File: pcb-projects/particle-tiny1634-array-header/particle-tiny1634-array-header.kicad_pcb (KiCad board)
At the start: 2 copper layers, 86.4 x 15.2 mm, 8 parts, among them P1 CHAIN1-TX, P2 CHAIN1-RX, P3 USB_A, P4 PWR-WEST, P5 PWR-EAST, P6 CHAIN2-TX, P7 CHAIN2-RX, P8 RS232

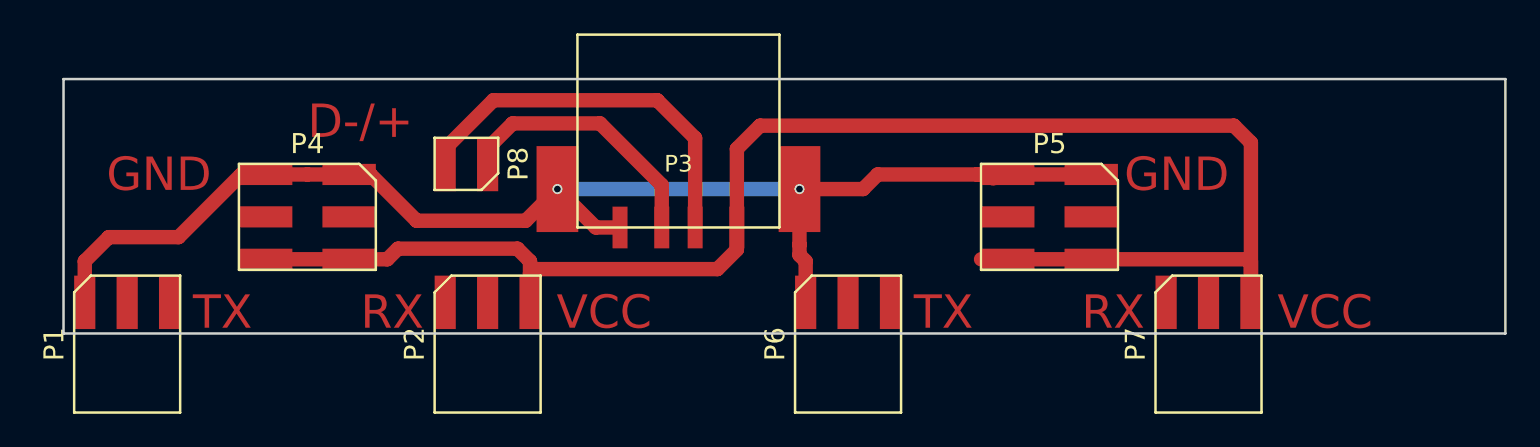
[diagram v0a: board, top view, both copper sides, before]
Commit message: minor edge cut alignment, added particle array
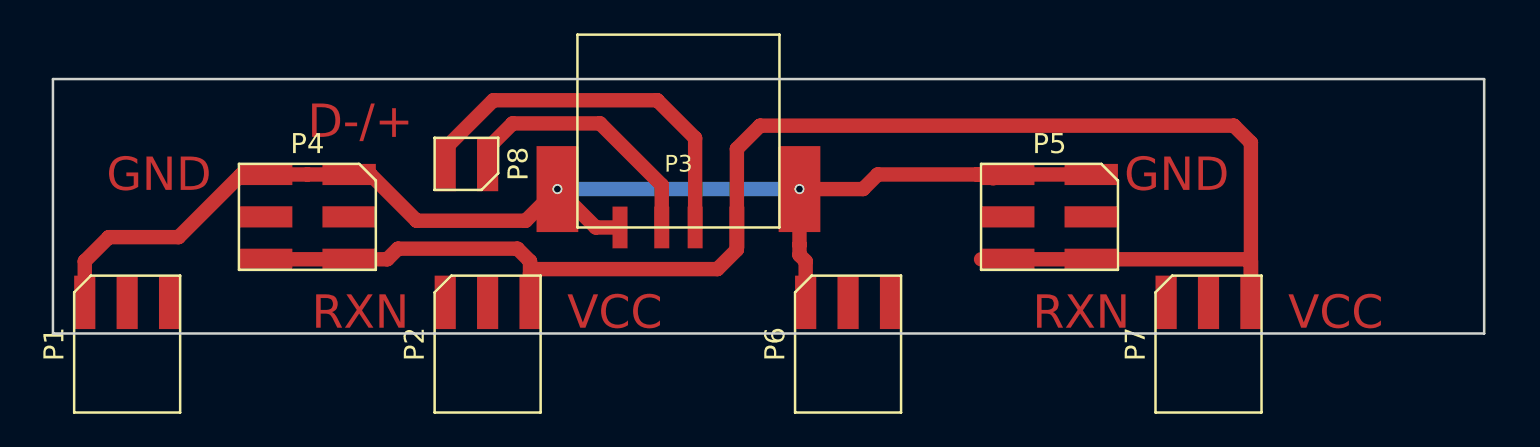
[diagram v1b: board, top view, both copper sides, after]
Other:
- board size 86.4 x 15.2 mm -> 85.7 x 15.2 mm
- board text added: "RXN"
- board text removed: "RX"
- board text removed: "TX"
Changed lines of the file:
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@@
     (links 16)
     (no_connects 0)
-    (area 27.864999 53.899999 114.375001 83.260001)
+    (area 25.98 50.909999 114.375001 74.355001)
     (thickness 1.6)
-    (drawings 13)
+    (drawings 11)
     (tracks 61)
     (zones 0)
@@
       (padsonsilk false)
       (subtractmaskfromsilk false)
-      (outputformat 1)
+      (outputformat 4)
       (mirror false)
-      (drillshape 1)
+      (drillshape 0)
       (scaleselection 1)
       (outputdirectory ""))
@@
     (effects (font (size 2 2) (thickness 0.4)))
   )
-  (gr_text RX (at 90.805 67.945) (layer F.Cu)
-    (effects (font (size 2 2) (thickness 0.4)))
-  )
-  (gr_text TX (at 80.645 67.945) (layer F.Cu)
-    (effects (font (size 2 2) (thickness 0.4)))
-  )
-  (gr_text RX (at 47.625 67.945) (layer F.Cu)
-    (effects (font (size 2 2) (thickness 0.4)))
-  )
-  (gr_text TX (at 37.465 67.945) (layer F.Cu)
-    (effects (font (size 2 2) (thickness 0.4)))
-  )
-  (gr_text VCC (at 60.325 67.945) (layer F.Cu)
+  (gr_text RXN (at 88.9 67.945) (layer F.Cu)
+    (effects (font (size 2 2) (thickness 0.4)))
+  )
+  (gr_text RXN (at 45.72 67.945) (layer F.Cu)
+    (effects (font (size 2 2) (thickness 0.4)))
+  )
+  (gr_text VCC (at 60.96 67.945) (layer F.Cu)
     (effects (font (size 2 2) (thickness 0.4)))
   )
@@
     (effects (font (size 2 2) (thickness 0.4)))
   )
-  (gr_text VCC (at 103.505 67.945) (layer F.Cu)
-    (effects (font (size 2 2) (thickness 0.4)))
-  )
-  (gr_line (start 27.94 53.975) (end 114.3 53.975) (layer Edge.Cuts) (width 0.15))
-  (gr_line (start 27.94 69.215) (end 114.3 69.215) (layer Edge.Cuts) (width 0.15))
-  (gr_line (start 114.3 69.215) (end 114.3 53.975) (layer Edge.Cuts) (width 0.15))
-  (gr_line (start 27.94 69.215) (end 27.94 53.975) (layer Edge.Cuts) (width 0.15))
+  (gr_text VCC (at 104.14 67.945) (layer F.Cu)
+    (effects (font (size 2 2) (thickness 0.4)))
+  )
+  (gr_line (start 27.305 53.975) (end 113.03 53.975) (layer Edge.Cuts) (width 0.15))
+  (gr_line (start 27.305 69.215) (end 113.03 69.215) (layer Edge.Cuts) (width 0.15))
+  (gr_line (start 113.03 69.215) (end 113.03 53.975) (layer Edge.Cuts) (width 0.15))
+  (gr_line (start 27.305 69.215) (end 27.305 53.975) (layer Edge.Cuts) (width 0.15))
   (segment (start 99.06 67.35) (end 99.06 57.785) (width 0.8636) (layer F.Cu) (net 1))
   (segment (start 99.06 57.785) (end 98.041705 56.766705) (width 0.8636) (layer F.Cu) (net 1))
